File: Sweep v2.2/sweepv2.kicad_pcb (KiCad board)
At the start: 2 copper layers, 216.9 x 86.9 mm, 51 parts, among them J1 AudioJack4dpb, J2 AudioJack4dpb, SW10 SW_Push, SW11 SW_Push, SW11_r1 SW_Push, SW12 SW_Push, SW12_r1 SW_Push, SW13_r1 SW_Push, SW14 SW_Push, SW15 SW_Push, SW15_r1 SW_Push, SW16 SW_Push, SW16_r1 SW_Push, SW17 SW_Push, SW17_r1 SW_Push, SW18 SW_Push, SW18_r1 SW_Push, SW2 SW_Push, SW20 SW_Push, SW20_r1 SW_Push, SW21 SW_Push, SW21_r1 SW_Push, SW2_r1 SW_Push, SW3 SW_Push, SW3_r1 SW_Push, SW4 SW_Push, SW4_r1 SW_Push, SW5 SW_Push, SW5_r1 SW_Push, SW6 SW_Push, SW6_r1 SW_Push, SW7_r1 SW_Push, SW8 SW_Push, SW8_r1 SW_Push, SW9 SW_Push, SW9_r1 SW_Push, U1 ProMicro-kbd, U2 ProMicro-kbd

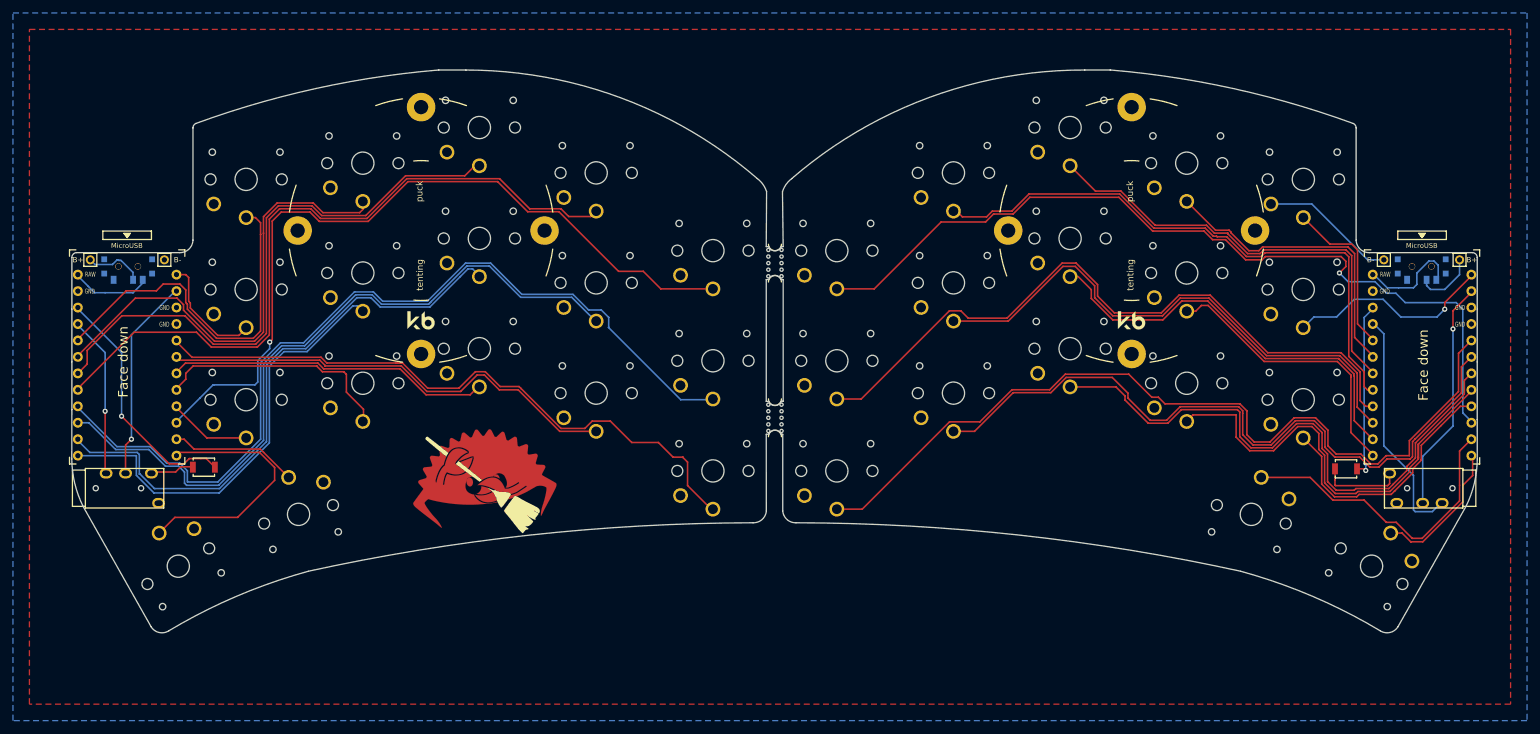
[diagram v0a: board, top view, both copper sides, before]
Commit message: Board shape updated
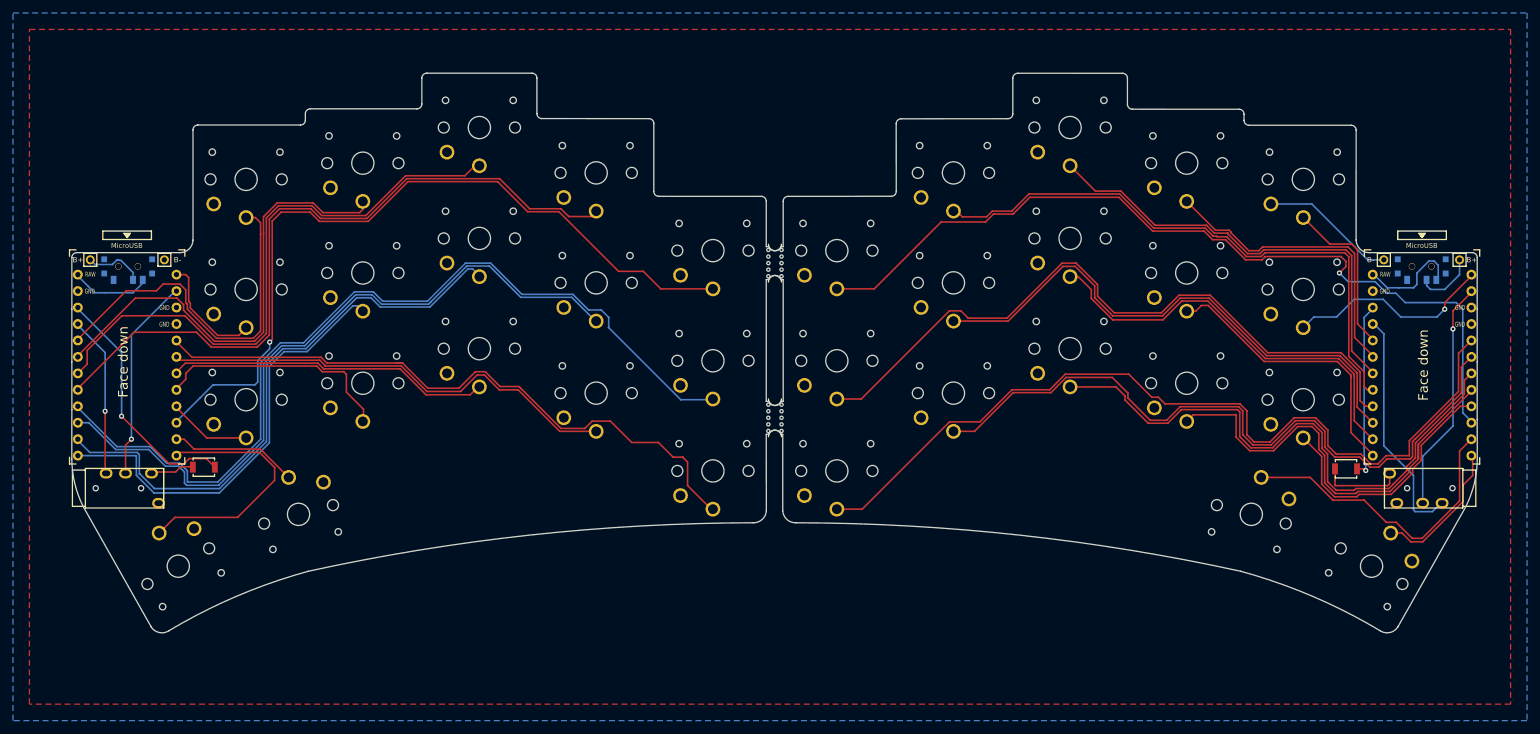
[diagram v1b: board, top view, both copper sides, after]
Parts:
- removed G***: LOGO, Kailh:ferris_broom
- removed REF** (x2): Tenting Puck, kbd:Tenting_Puck2
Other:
- board size 216.9 x 86.9 mm -> 216.9 x 86.4 mm
